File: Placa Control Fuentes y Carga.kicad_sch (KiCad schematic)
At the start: 70 parts, among them J1 TBP01R1-508-02BE, J10 TBP01R1-508-02BE, J2 TBP01R1-508-02BE, J3 TBP01R1-508-02BE, J4 TBP01R1-508-02BE, J5 TBP01R1-508-02BE, J6 TBP01R1-508-02BE, J7 TBP01R1-508-02BE, J8 TBP01R1-508-02BE, J9 TBP01R1-508-02BE, Q1 BC558, Q2 BC558, Q3 2N3904, Q4 IRF9540N, Q5 IRF5305, U1 LM2596S_Modulo_Regulable, U2 ACS724LLCTR-05AB-T, U2 Arduino_Nano_ATmega328P, U3 ACS724LLCTR-05AB-T, U4 MAX485E, U5 4N35, U6 Relay_Module_WB-083

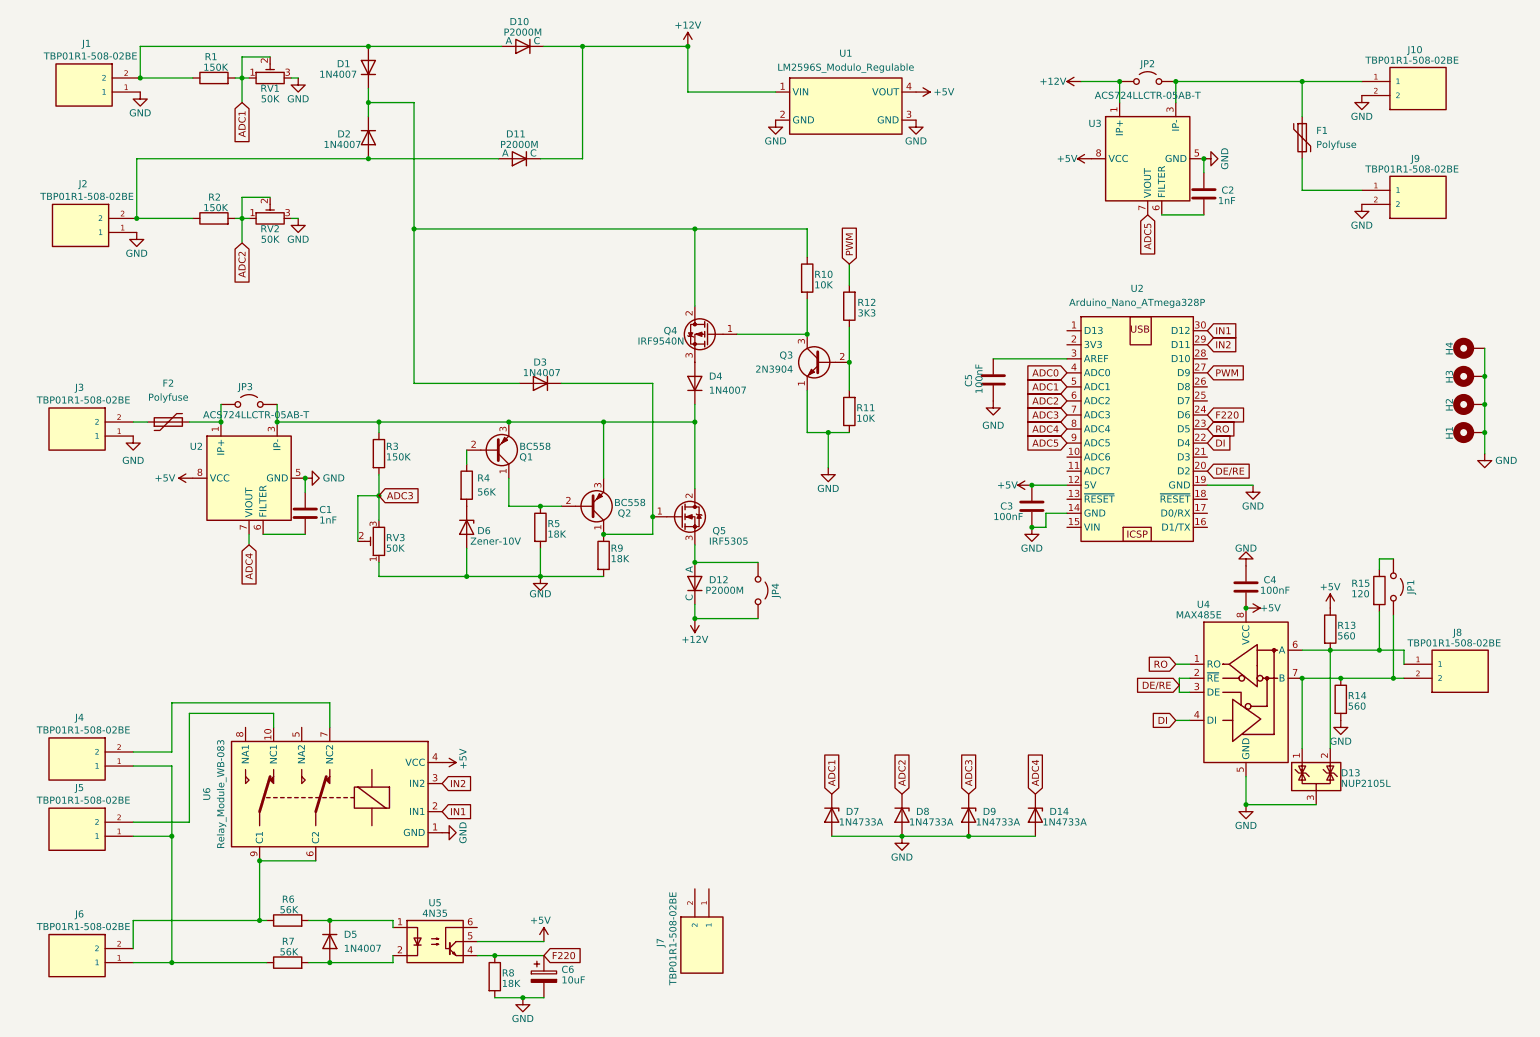
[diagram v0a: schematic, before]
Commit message: Siguen las actualizaciones. Siguiente paso: Faltan asociar footprints a muchos símbolos. Tengo que ver la asignaciones hechas en los proyectos anteriores, listarlos y con esa información podré completar la lista de asignación de huellas. También falta hacer el footprint para el "Relay_Module_WB-083".
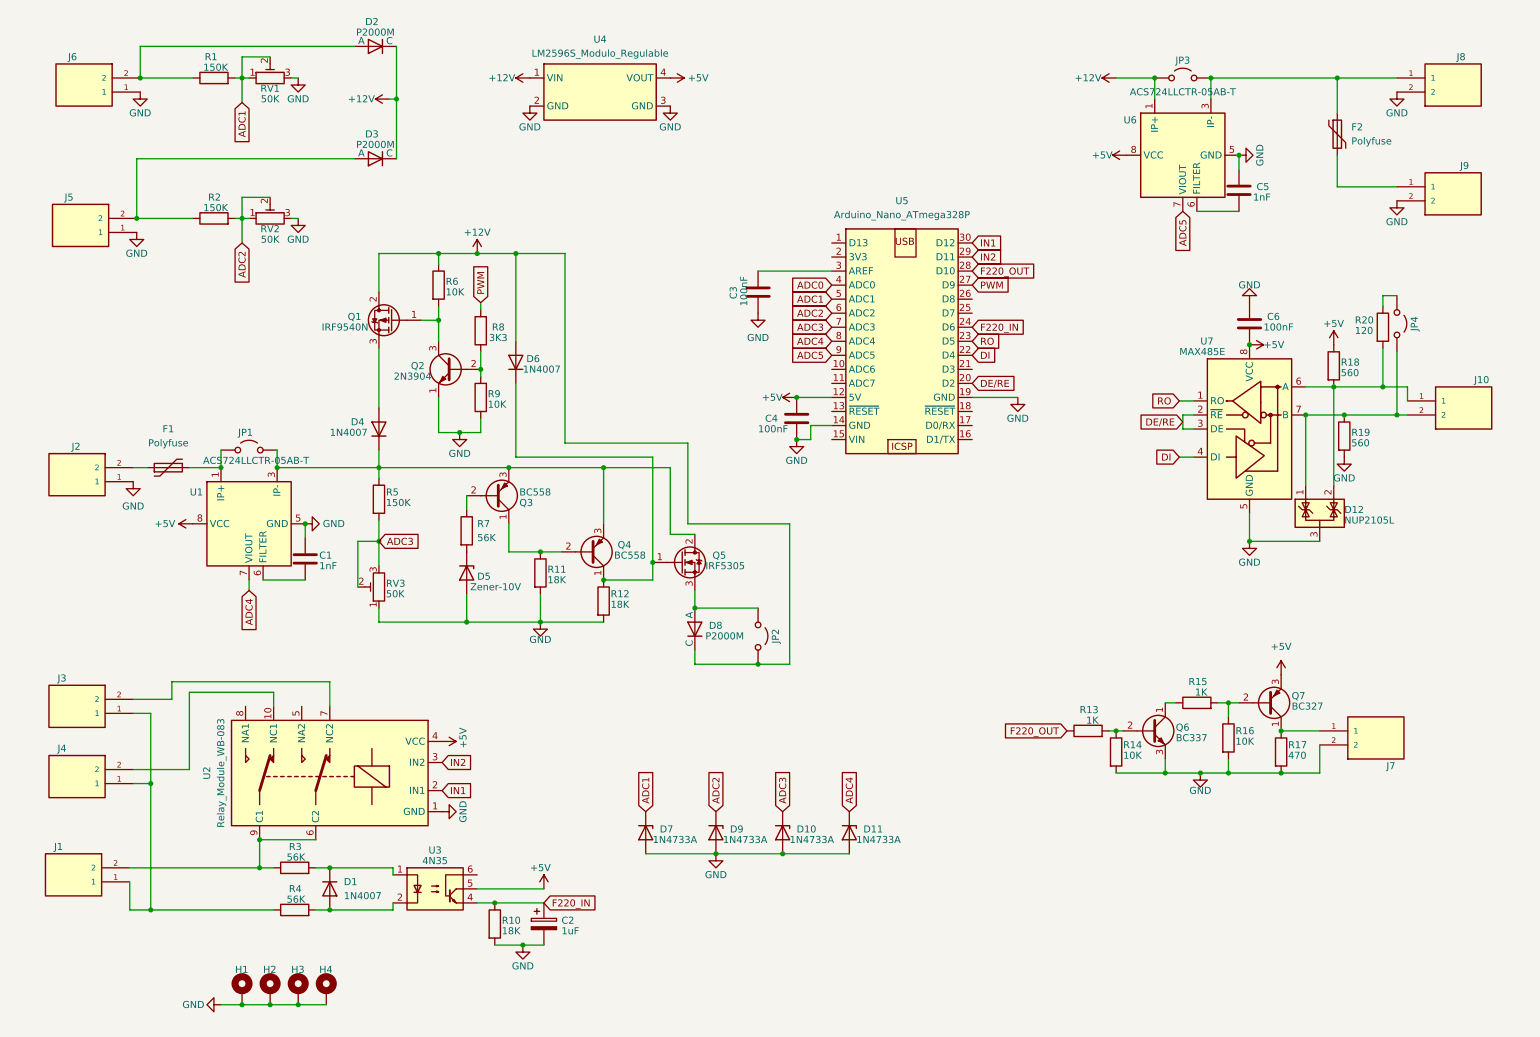
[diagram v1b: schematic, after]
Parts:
- removed D1, D2, D3: 1N4007, Diode_THT:D_DO-41_SOD81_P10.16mm_Horizontal, symbol Diode:1N4007
- added D6: 1N4007, Diode_THT:D_DO-41_SOD81_P10.16mm_Horizontal, symbol Diode:1N4007
- added Q6: BC337, Package_TO_SOT_THT:TO-92_Inline, symbol Simbolos2:BC337
- added Q7: BC327, Package_TO_SOT_THT:TO-92_Inline, symbol Simbolos2:BC327
- added R13, R15: 1K, symbol Device:R
- added R14, R16: 10K, symbol Device:R
- added R17: 470, symbol Device:R
- C2: renamed from C6; value 10uF -> 1uF
- renumbered C5 to C3, C3 to C4, C2 to C5, C4 to C6, D5 to D1, D9 to D10, D14 to D11, D13 to D12, D10 to D2, D11 to D3, D6 to D5, D12 to D8, D8 to D9, F2 to F1, F1 to F2, J6 to J1, J8 to J10, J3 to J2, J4 to J3, J5 to J4, J2 to J5, J1 to J6, J10 to J8, JP3 to JP1, JP4 to JP2, JP2 to JP3, JP1 to JP4, Q4 to Q1, Q3 to Q2, Q1 to Q3, Q2 to Q4, R8 to R10, R5 to R11, R9 to R12, R13 to R18, R14 to R19, R15 to R20, R6 to R3, R7 to R4, R3 to R5, R10 to R6, R4 to R7, R12 to R8, R11 to R9, U2 to U1, U6 to U2, U5 to U3, U1 to U4, U2 to U5, U3 to U6, U4 to U7
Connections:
- net +12V: now also Q1.2 (D), R6.1, D6.2 (A)
- net +5V: now also Q7.3 (E)
- net GND: now also J7.2, Q6.3 (E), R14.2, R16.2, R17.2
- net at Q4.1 (C), Q5.1 (G), R12.1: now also D6.1 (K)
- net F220_OUT: now reaches U5.28 (D10)
- net F220_OUT: now also R13.1
- net at J7.1: now also Q7.1 (C), R17.1
- net F220 renamed F220_IN
- new net: Q7.2 (B), R15.2, R16.1
- new net: Q6.1 (C), R15.1
- new net: Q6.2 (B), R13.2, R14.1
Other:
- company: (none) -> EYSE S.A.C.I.
- title: (none) -> Placa Controladora de Fuentes y Carga
- moved on the sheet: C1, C2, C3, C4, C5, C6, D1, D10, D11, D12, D2, D3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

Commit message: Hacemos backup por las dudas de las pequeñas modificaciones realizadas. Lo que sigue es hacer toda la interface RS485 aislada, protegida, igual que con la placa expansora de ocho relés.
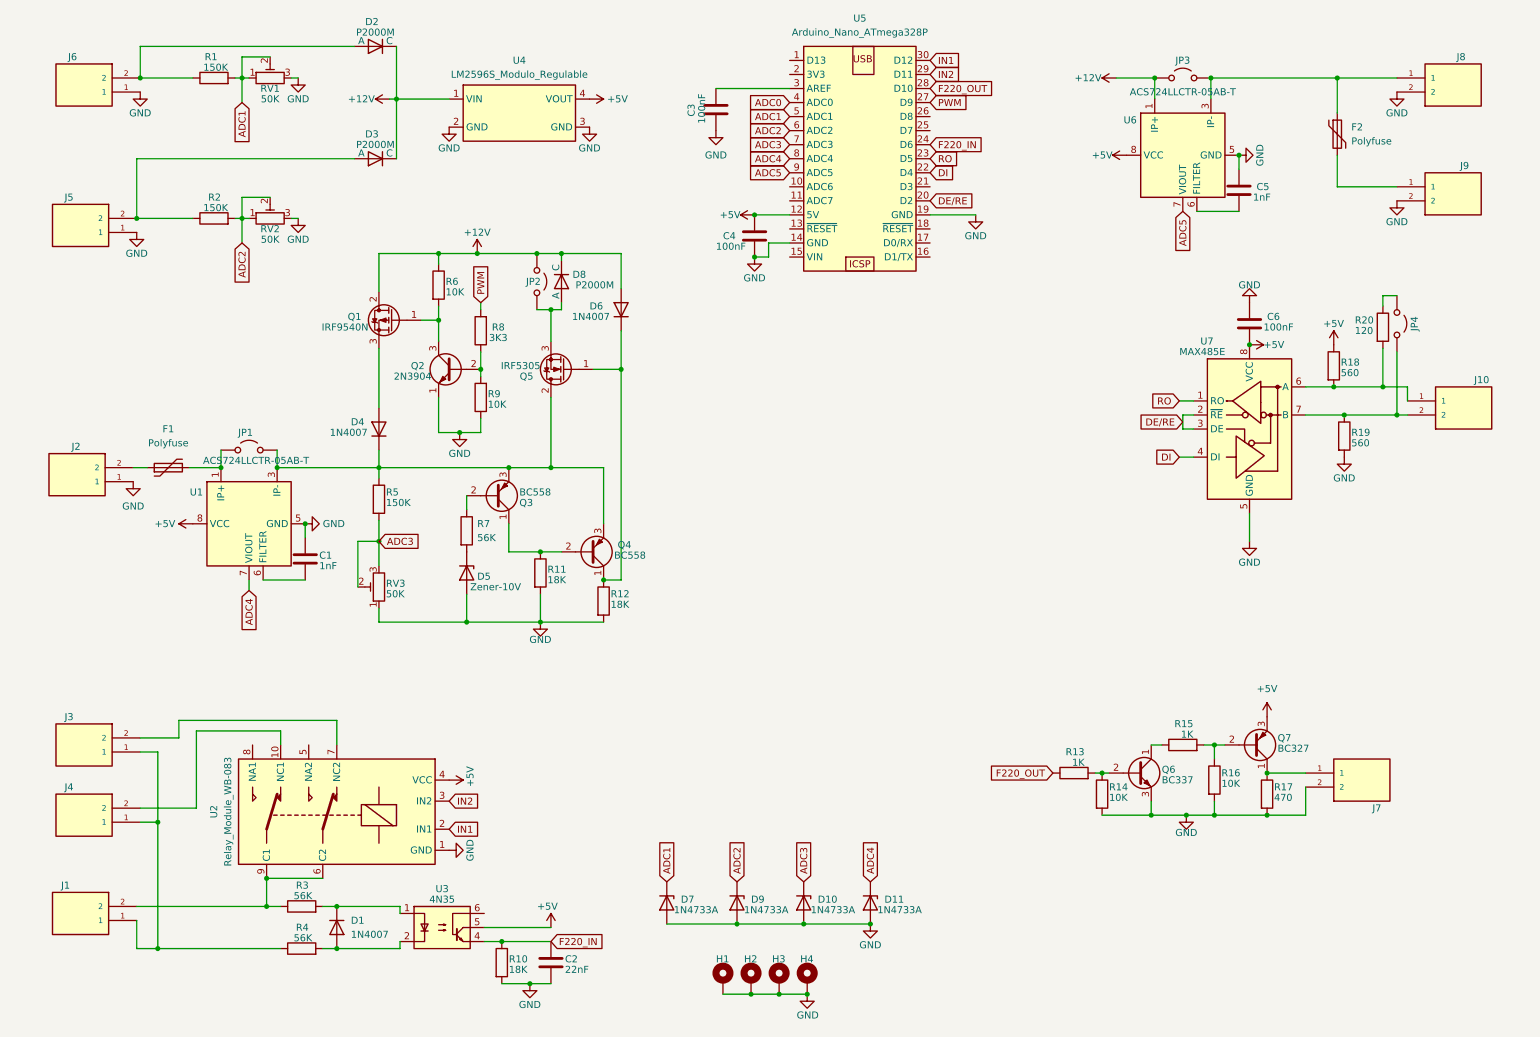
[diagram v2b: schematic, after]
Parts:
- removed C2: 1uF, symbol Device:C_Polarized
- removed D12: NUP2105L, Package_TO_SOT_SMD:SOT-23, symbol Simbolos2:NUP2105L
- added C2: 22nF, Capacitor_THT:C_Disc_D5.0mm_W2.5mm_P5.00mm, symbol Device:C
- C1, C3, C4, C5, C6: footprint (none) -> Capacitor_THT:C_Disc_D5.0mm_W2.5mm_P5.00mm
- D2, D3, D8: footprint (none) -> Diode_THT:D_P600_R-6_P15.24mm_Horizontal
- D5: footprint (none) -> Diode_THT:D_DO-35_SOD27_P7.62mm_Horizontal
- F1, F2: footprint (none) -> Fuse:Fuse_Bourns_MF-R500
- H1, H2, H3, H4: footprint (none) -> MountingHole:MountingHole_3.2mm_M3_Pad
- J1, J10, J2, J3, J4, J5, J6, J7, J8, J9: footprint TerminalBlock_Phoenix:TerminalBlock_Phoenix_PT-1,5-2-5.0-H_1x02_P5.00mm_Horizontal -> TerminalBlock_Phoenix:TerminalBlock_Phoenix_MKDS-1,5-2-5.08_1x02_P5.08mm_Horizontal
- JP1, JP2, JP3, JP4: footprint (none) -> Connector_PinHeader_2.54mm:PinHeader_1x02_P2.54mm_Vertical
- Q3, Q4, Q6, Q7: footprint Package_TO_SOT_THT:TO-92_Inline -> Package_TO_SOT_THT:TO-92_Inline_Wide_CBE
- R1, R10, R11, R12, R13, R14, R15, R16, R17, R18, R19, R2, R20, R3, R4, R5, R6, R7, R8, R9, RV1, RV2, RV3: footprint (none) -> Resistor_THT:R_Axial_DIN0207_L6.3mm_D2.5mm_P7.62mm_Horizontal
- U4: footprint Package_LM2596_Regulable -> Damian_PCB:Modulo Step Down Regulable LM2596
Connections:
- net +12V: now also JP2.1 (A); no longer JP2.2 (B)
- net F220_IN: now also C2.1
- net GND: now also C2.2
- net at D8.1 (A), Q5.3 (S): now also JP2.2 (B); no longer JP2.1 (A)
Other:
- moved on the sheet: C3, C4, D1, D10, D11, D7, D9, H1, H2, H3, H4, J1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

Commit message: Ya se completaron diria el total de los footprints para cada símbolo. Falta hacer una revisión general más detallada y luego pasar al PCB directo.
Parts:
- added C10, C11: F102K43Y5RP6UK5R, Damian_PCB:CAP_F_11X5P_VIS, symbol Device:C
- added C12, C8, C9: 100nF, Capacitor_THT:C_Disc_D5.0mm_W2.5mm_P2.50mm, symbol Device:C
- added C13, C14: 10uF, Capacitor_THT:CP_Radial_D5.0mm_P2.00mm, symbol Device:C_Polarized
- added C7: F102K43Y5RP6UK5R, Damian_PCB:CAP_F_11X5P_VIS, symbol Simbolos1:Cap_Y
- added D12: SM712, Package_TO_SOT_SMD:SOT-23_Handsoldering, symbol Simbolos1:SM712
- added D13, D14: SA12CA, Damian_PCB:DO-204AC_SA, symbol Simbolos1:SMAJ12CA
- added D15: SA6.5CA, Damian_PCB:DO-204AC_SA, symbol Simbolos1:SMAJ12CA
- added F3, F4: MF-R030, Fuse:Fuse_Bourns_MF-RHT050, symbol Simbolos1:NANOSMDCH030F/24-02
- added GD1: 2036-15-B2LF, Fuse:GDT_Yageo_3RxxxxL-6, symbol Simbolos1:2038-15-SM-RPLF
- added J11: TBP01R1-508-03BE, Damian_PCB:CUI_TBP01R1-508-03BE, symbol Simbolos1:TBP01R1-508-03BE
- added R21: 1M, Resistor_THT:R_Axial_DIN0207_L6.3mm_D2.5mm_P7.62mm_Horizontal, symbol Device:R
- added TP1, TP10, TP11, TP12, TP2, TP3, TP4, TP5, TP6, TP7, TP8, TP9: TestPoint, TestPoint:TestPoint_THTPad_D2.5mm_Drill1.2mm, symbol Connector:TestPoint
- added U8: MAX22445FAWE+, Package_SO:SOIC-16W_7.5x10.3mm_P1.27mm, symbol Simbolos1:MAX22445FAWE+
- added U9: RI3-0505S, Damian_PCB:CONV_RI3-0505S, symbol Simbolos1:MEE1S0303SC
- C1, C2, C3, C4, C5, C6: footprint Capacitor_THT:C_Disc_D5.0mm_W2.5mm_P5.00mm -> Capacitor_THT:C_Disc_D5.0mm_W2.5mm_P2.50mm
- D2, D3, D8: footprint Diode_THT:D_P600_R-6_P15.24mm_Horizontal -> Damian_PCB:D_P600_R-6_P15.24mm_Horizontal
- F1: value Polyfuse -> Polyfuse MF-R500; footprint Fuse:Fuse_Bourns_MF-R500 -> Fuse:Fuse_Bourns_MF-RHT500
- F2: value Polyfuse -> Polyfuse MF-R250; footprint Fuse:Fuse_Bourns_MF-R500 -> Fuse:Fuse_Bourns_MF-RHT300
- Q3, Q4, Q6, Q7: footprint Package_TO_SOT_THT:TO-92_Inline_Wide_CBE -> Package_TO_SOT_THT:TO-92_HandSolder
- U2: footprint (none) -> Damian_PCB:Relay_Module_WB-083
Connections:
- net +5V: now also C10.2, C13.1, C8.1, TP3.1, U8.1 (VDDA), U8.7 (ENA), U9.2 (+Vin); no longer C6.2, R18.1, U7.8 (VCC)
- net ADC1: now also TP12.1
- net ADC2: now also TP11.1
- net DE/RE: now also TP8.1, U8.3 (IN1); no longer U7.2 (~{RE}), U7.3 (DE)
- net DI: now also TP9.1, U8.4 (IN2); no longer U7.4 (DI)
- net GND: now also C11.2, C13.2, C8.2, TP4.1, U8.2 (GNDA), U8.8 (GNDA), U9.1 (-Vin); no longer C6.1, H1.1, H2.1, H3.1, H4.1, R19.2, U7.5 (GND)
- net RO: now also TP10.1, U8.6 (OUT4); no longer U7.1 (RO)
- net at R18.2, R20.2, U7.6 (A): now also D12.2 (K), D14.1 (K), D15.1 (K), F3.1; no longer J10.1
- net at JP4.2 (B), R19.1, U7.7 (B): now also D12.1 (K), D13.1 (K), D15.2 (A), F4.1; no longer J10.2
- new net: TP7.1, U7.2 (~{RE}), U7.3 (DE), U8.14 (OUT1)
- new net: F3.2, GD1.1 (A+), J11.1
- new net: F4.2, GD1.3 (B-), J11.3
- new net: TP5.1, U7.1 (RO), U8.11 (IN4)
- new net: TP6.1, U7.4 (DI), U8.13 (OUT2)
- new net +5V_B: C10.1, C12.1, C14.1, C6.2, C9.2, R18.1, TP1.1, U7.8 (VCC), U8.10 (ENB), U8.16 (VDDB), U9.4 (+Vout)
- new net Earth: C7.2, D12.3 (A), D13.2 (A), D14.2 (A), GD1.2 (GND), H1.1, H2.1, H3.1, H4.1, J11.2, R21.1
- new net GND_B: C11.1, C12.2, C14.2, C6.1, C7.1, C9.1, R19.2, R21.2, TP2.1, U7.5 (GND), U8.15 (GNDB), U8.9 (GNDB), U9.3 (-Vout)
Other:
- moved on the sheet: C5, C6, F2, J10, J7, J8, J9, JP3, JP4, Q6, Q7, R13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

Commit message: Más actualizaciones en el sch antes de pasar al PCB.
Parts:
- added TP14, TP15, TP16, TP17, TP18, TP19, TP20, TP21, TP22, TP23, TP24, TP25: TestPoint, TestPoint:TestPoint_THTPad_D2.5mm_Drill1.2mm, symbol Connector:TestPoint
- F2: footprint Fuse:Fuse_Bourns_MF-RHT300 -> Damian_PCB:FUSE_MF-R250_BRN
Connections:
- net ADC1: now also TP11.1; no longer TP12.1
- net ADC2: now also TP12.1; no longer TP11.1
- net ADC3: now also TP14.1
- net ADC4: now also TP16.1
- net F220_IN: now also TP15.1
- net IN1: now also TP19.1
- net IN2: now also TP20.1
- net at Q1.1 (G), Q2.3 (C), R6.2: now also TP21.1
- net at D1.1 (K), R3.2, U3.1: now also TP17.1
- net at D1.2 (A), R4.2, U3.2: now also TP18.1
- net at F1.1, J2.2: now also TP25.1
- net at D6.1 (K), Q4.1 (C), Q5.1 (G)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: now also TP22.1
- net at Q3.1 (C), Q4.2 (B), R11.1: now also TP23.1
- net at Q3.2 (B), R7.1: now also TP24.1
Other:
- moved on the sheet: R1, R2, TP3, TP4

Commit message: Se hicieron muchas correcciones en el circuito y en los footprints del PCB. Esto es solo para guardar un respaldo.
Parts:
- removed F1: Polyfuse MF-R500, Fuse:Fuse_Bourns_MF-RHT500, symbol Device:Polyfuse
- removed J10: TBP01R1-508-02BE, TerminalBlock_Phoenix:TerminalBlock_Phoenix_MKDS-1,5-2-5.08_1x02_P5.08mm_Horizontal, symbol TBP01R1-508-02BE:TBP01R1-508-02BE
- added C15, C23: 470µF/35V low-ESR, Damian_PCB:CAP_UAQ_10X20_NCH, symbol Simbolos1:UPW1V471MPD1TD
- added C17, C21: 10µF/25V, Capacitor_THT:CP_Radial_D5.0mm_P2.00mm, symbol Device:C_Polarized
- added C18: 100µF/25V, Capacitor_THT:CP_Radial_D5.0mm_P2.00mm, symbol Device:C_Polarized
- added C19, C20, C22, C24, C25: 100nF, Capacitor_THT:C_Disc_D5.0mm_W2.5mm_P2.50mm, symbol Device:C
- added CR1, CR2: SMBJ18A, Damian_PCB:DIODE_DO214AA, symbol Simbolos1:SMBJ18A
- added CR3: SMBJ16A, Damian_PCB:DIODE_DO214AA, symbol Simbolos1:SMBJ18A
- added F1: ETA 1610-H2-7.5A, Damian_PCB:FuseHolder_Blade_ATO_Littelfuse_FLR_178.6165, symbol Device:Fuse
- added F5, F6: ETA 1610-H2-5A, Damian_PCB:FuseHolder_Blade_ATO_Littelfuse_FLR_178.6165, symbol Device:Fuse
- added R22, R23: 47, Resistor_THT:R_Axial_DIN0207_L6.3mm_D2.5mm_P7.62mm_Horizontal, symbol Device:R
- added R24, R25: B72214S0271K101, VARS_B72214S0271K101_TDK, symbol Simbolos1:B72214S0271K101
- F2: value Polyfuse MF-R250 -> Polyfuse MF-R500; footprint Damian_PCB:FUSE_MF-R250_BRN -> Damian_PCB:FUSE_MF-R500_BRN
- J10: renamed from J11; footprint Damian_PCB:CUI_TBP01R1-508-03BE -> Damian_PCB:TerminalBlock_Phoenix_MKDS-1,5-2-5.08_1x03_P5.08mm_Horizontal
- R3, R4: value 56K -> 56K 0.5W; footprint Resistor_THT:R_Axial_DIN0207_L6.3mm_D2.5mm_P7.62mm_Horizontal -> Resistor_THT:R_Axial_DIN0309_L9.0mm_D3.2mm_P12.70mm_Horizontal
- RV1, RV2, RV3: footprint Resistor_THT:R_Axial_DIN0207_L6.3mm_D2.5mm_P7.62mm_Horizontal -> Potentiometer_THT:Potentiometer_Bourns_3296W_Vertical
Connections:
- net +5V: now also C3.1, U5.3 (AREF), C24.2, C25.2
- net GND: now also U8.5 (IN3), C15.2, C17.2, C18.2, C19.2, C20.1, C21.2, C22.1, C23.2, C24.1, C25.1, CR1.2, CR2.2, CR3.2
- net at Q2.3 (C), R6.2, TP21.1: now also R22.1; no longer Q1.1 (G)
- net at D4.1 (K), JP1.2 (B), Q3.3 (E)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: now also C18.1, C20.2
- net at J2.2: now also F1.1; no longer TP25.1
- net at F2.1, JP3.2 (B), U6.3 (IP-)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: no longer J8.1
- net at D6.1 (K), Q4.1 (C), R12.1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: now also R23.1; no longer Q5.1 (G)
- net at JP1.1 (A), U1.1 (IP+), U1.2 (IP+): now also TP25.1, CR3.1, F1.2
- net at D3.1 (A), R2.1: now also C21.1, C22.2, C23.1, CR2.1, F6.2; no longer J5.2
- net at D2.1 (A), R1.1: now also C15.1, C17.1, C19.1, CR1.1, F5.2; no longer J6.2
- net at F2.2, J9.1: now also J8.1
- new net: Q1.1 (G), R22.2
- new net: F6.1, J5.2
- new net: F5.1, J6.2
- new net: Q5.1 (G), R23.2
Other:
- moved on the sheet: C10, C11, C12, C13, C14, C2, C7, D1, D10, D11, D2, D3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
